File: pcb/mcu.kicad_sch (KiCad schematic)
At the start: 32 parts, among them J1 Conn_01x02_Pin, SW2 SW_Push, SW3 SW_SPDT, U1 TLV1117LV33DCYR, U2 W25Q64JVSSIQ_C179171, U3 STM32H750VBTx, Y1 25 MHz

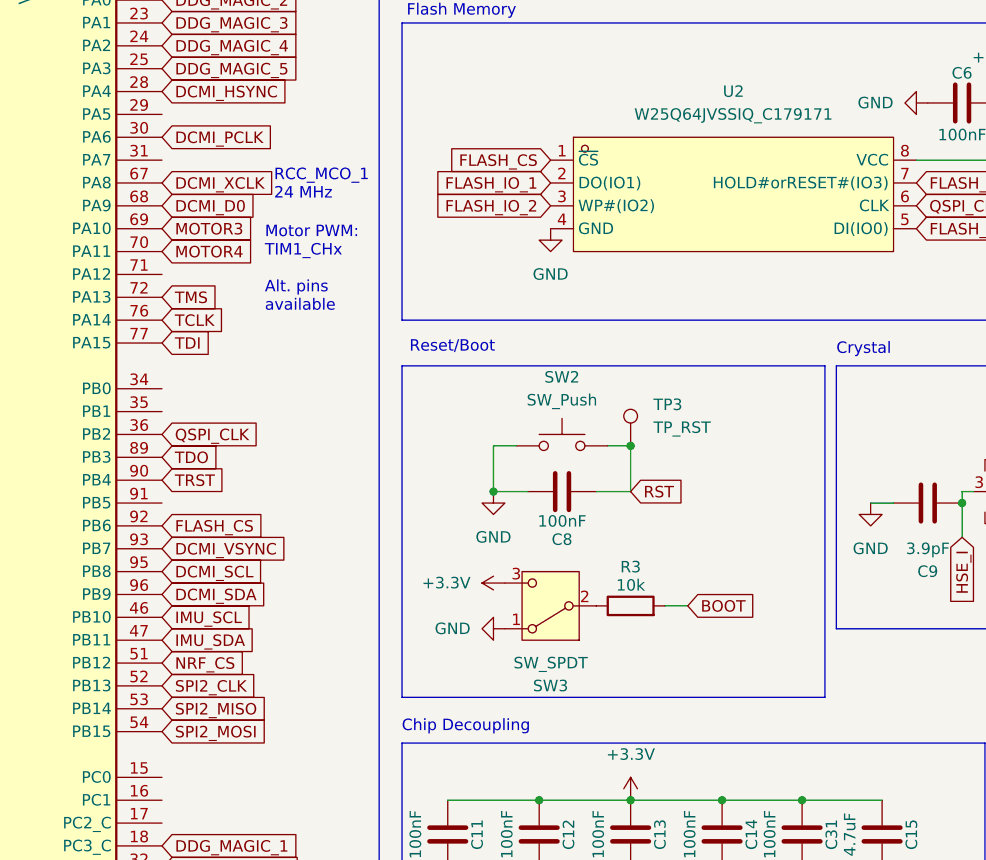
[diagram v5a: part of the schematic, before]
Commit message: [pcb] changed switches to optimize pcb layout
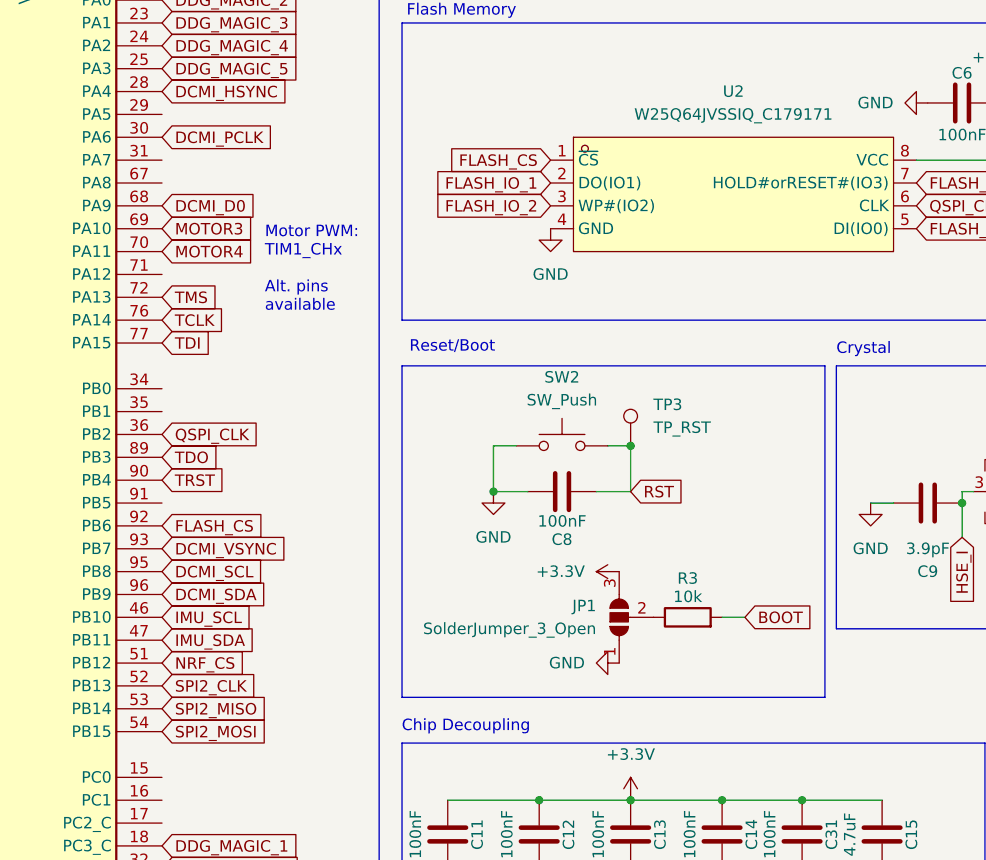
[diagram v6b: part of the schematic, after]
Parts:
- removed SW3: SW_SPDT, Button_Switch_THT:SW_Slide-03_Wuerth-WS-SLTV_10x2.5x6.4_P2.54mm, symbol Switch:SW_SPDT
- added JP1: SolderJumper_3_Open, Jumper:SolderJumper-3_P1.3mm_Open_RoundedPad1.0x1.5mm, symbol Jumper:SolderJumper_3_Open
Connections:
- net +3.3V: now also JP1.3 (B)
- net GND: now also JP1.1 (A)
- net at R3.1: now also JP1.2 (C)
- net DCMI_XCLK: no longer names the net of U3.67 (PA8)
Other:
- note removed: "RCC_MCO_1 24 MHz"
- moved on the sheet: R3
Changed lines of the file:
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@@
 		)
 	)
-	(text "RCC_MCO_1\n24 MHz"
-		(exclude_from_sim no)
-		(at 100.076 66.294 0)
-		(effects
-			(font
-				(size 1.27 1.27)
-				(color 194 0 194 1)
-			)
-			(justify left)
-		)
-	)
 	(text "SPI pins can be moved around\n\n(page 78 of datasheet)"
 		(exclude_from_sim no)
@@
 	(wire
 		(pts
-			(xy 143.51 113.03) (xy 146.05 113.03)
+			(xy 149.86 114.3) (xy 152.4 114.3)
 		)
 		(stroke
@@
 	(global_label "BOOT"
 		(shape input)
-		(at 146.05 113.03 0)
+		(at 152.4 114.3 0)
 		(fields_autoplaced yes)
 		(effects
@@
 		)
 		(property "Intersheetrefs" "${INTERSHEET_REFS}"
-			(at 153.9338 113.03 0)
+			(at 160.2838 114.3 0)
 			(effects
 				(font
@@
 		)
 	)
-	(global_label "DCMI_XCLK"
-		(shape input)
-		(at 87.63 66.04 0)
-		(fields_autoplaced yes)
-		(effects
-			(font
-				(size 1.27 1.27)
-			)
-			(justify left)
-		)
-		(property "Intersheetrefs" "${INTERSHEET_REFS}"
-			(at 100.9566 66.04 0)
-			(effects
-				(font
-					(size 1.27 1.27)
-				)
-				(justify left)
-				(hide yes)
-			)
-		)
-	)
 	(global_label "FLASH_IO_3"
 		(shape input)
@@
 	(symbol
 		(lib_id "power:GND")
-		(at 125.73 115.57 270)
+		(at 138.43 119.38 270)
 		(unit 1)
 		(exclude_from_sim no)
@@
 		(fields_autoplaced yes)
 		(property "Reference" "#PWR025"
-			(at 119.38 115.57 0)
+			(at 132.08 119.38 0)
 			(effects
 				(font
@@
 		)
 		(property "Value" "GND"
-			(at 121.92 115.5699 90)
+			(at 134.62 119.3799 90)
 			(effects
 				(font
@@
 		)
 		(property "Footprint" ""
-			(at 125.73 115.57 0)
+			(at 138.43 119.38 0)
 			(effects
 				(font
@@
 		)
 		(property "Datasheet" ""
-			(at 125.73 115.57 0)
+			(at 138.43 119.38 0)
 			(effects
 				(font
@@
 		)
 		(property "Description" "Power symbol creates a global label with name \"GND\" , ground"
-			(at 125.73 115.57 0)
+			(at 138.43 119.38 0)
 			(effects
 				(font
@@
 	)
 	(symbol
+		(lib_id "Jumper:SolderJumper_3_Open")
+		(at 138.43 114.3 90)
+		(unit 1)
+		(exclude_from_sim no)
+		(in_bom no)
+		(on_board yes)
+		(dnp no)
+		(fields_autoplaced yes)
+		(property "Reference" "JP1"
+			(at 135.89 113.0299 90)
+			(effects
+				(font
+					(size 1.27 1.27)
+				)
+				(justify left)
+			)
+		)
+		(property "Value" "SolderJumper_3_Open"
+			(at 135.89 115.5699 90)
+			(effects
+				(font
+					(size 1.27 1.27)
+				)
+				(justify left)
+			)
+		)
+		(property "Footprint" "Jumper:SolderJumper-3_P1.3mm_Open_RoundedPad1.0x1.5mm"
+			(at 138.43 114.3 0)
+			(effects
+				(font
+					(size 1.27 1.27)
+				)
+				(hide yes)
+			)
+		)
+		(property "Datasheet" "~"
+			(at 138.43 114.3 0)
+			(effects
+				(font
+					(size 1.27 1.27)
+				)
+				(hide yes)
+			)
+		)
+		(property "Description" "Solder Jumper, 3-pole, open"
+			(at 138.43 114.3 0)
+			(effects
+				(font
+					(size 1.27 1.27)
+				)
+				(hide yes)
+			)
+		)
+		(pin "1"
+		)
+		(pin "2"
+		)
+		(pin "3"
+		)
+		(instances
+			(project ""
+				(path "/c0be3de2-9de4-4447-aa6f-537ea5f31aac/0c8c942c-f992-4664-b7a3-b87cb51e1584"
+					(reference "JP1")
+					(unit 1)
+				)
+			)
+		)
+	)
+	(symbol
 		(lib_id "power:GND")
 		(at 130.81 71.12 0)
@@
 	(symbol
 		(lib_id "power:+3.3V")
-		(at 125.73 110.49 90)
+		(at 138.43 109.22 90)
 		(unit 1)
 		(exclude_from_sim no)
@@
 		(fields_autoplaced yes)
 		(property "Reference" "#PWR072"
-			(at 129.54 110.49 0)
+			(at 142.24 109.22 0)
 			(effects
 				(font
@@
 		)
 		(property "Value" "+3.3V"
-			(at 121.92 110.4899 90)
+			(at 134.62 109.2199 90)
 			(effects
 				(font
@@
 		)
 		(property "Footprint" ""
-			(at 125.73 110.49 0)
+			(at 138.43 109.22 0)
 			(effects
 				(font
@@
 		)
 		(property "Datasheet" ""
-			(at 125.73 110.49 0)
+			(at 138.43 109.22 0)
 			(effects
 				(font
@@
 		)
 		(property "Description" "Power symbol creates a global label with name \"+3.3V\""
-			(at 125.73 110.49 0)
+			(at 138.43 109.22 0)
 			(effects
 				(font
@@
 	(symbol
 		(lib_id "Device:R")
-		(at 139.7 113.03 90)
+		(at 146.05 114.3 90)
 		(unit 1)
 		(exclude_from_sim no)
@@
 		(dnp no)
 		(property "Reference" "R3"
-			(at 139.7 108.712 90)
+			(at 146.05 109.982 90)
 			(effects
 				(font
@@
 		)
 		(property "Value" "10k"
-			(at 139.7 110.744 90)
+			(at 146.05 112.014 90)
 			(effects
 				(font
@@
 		)
 		(property "Footprint" "Resistor_SMD:R_0805_2012Metric_Pad1.20x1.40mm_HandSolder"
-			(at 139.7 114.808 90)
+			(at 146.05 116.078 90)
 			(effects
 				(font
@@
 		)
 		(property "Datasheet" "~"
-			(at 139.7 113.03 0)
+			(at 146.05 114.3 0)
 			(effects
 				(font
@@
 		)
 		(property "Description" "Resistor"
-			(at 139.7 113.03 0)
+			(at 146.05 114.3 0)
 			(effects
 				(font
@@
 					(unit 1)
 				)
-			)
-		)
-	)
-	(symbol
-		(lib_id "Switch:SW_SPDT")
-		(at 130.81 113.03 180)
-		(unit 1)
-		(exclude_from_sim no)
-		(in_bom yes)
-		(on_board yes)
-		(dnp no)
-		(property "Reference" "SW3"
-			(at 130.81 121.92 0)
-			(effects
-				(font
-					(size 1.27 1.27)
-				)
-			)
-		)
-		(property "Value" "SW_SPDT"
-			(at 130.81 119.38 0)
-			(effects
-				(font
-					(size 1.27 1.27)
-				)
-			)
-		)
-		(property "Footprint" "Button_Switch_THT:SW_Slide-03_Wuerth-WS-SLTV_10x2.5x6.4_P2.54mm"
-			(at 130.81 113.03 0)
-			(effects
-				(font
-					(size 1.27 1.27)
-				)
-				(hide yes)
-			)
-		)
-		(property "Datasheet" "~"
-			(at 130.81 105.41 0)
-			(effects
-				(font
-					(size 1.27 1.27)
-				)
-				(hide yes)
-			)
-		)
-		(property "Description" "Switch, single pole double throw"
-			(at 130.81 113.03 0)
-			(effects
-				(font
-					(size 1.27 1.27)
-				)
-				(hide yes)
-			)
-		)
-		(pin "2"
-		)
-		(pin "3"
-		)
-		(pin "1"
-		)
-		(instances
-			(project "astra"
-				(path "/c0be3de2-9de4-4447-aa6f-537ea5f31aac/0c8c942c-f992-4664-b7a3-b87cb51e1584"
-					(reference "SW3")
-					(unit 1)
-				)

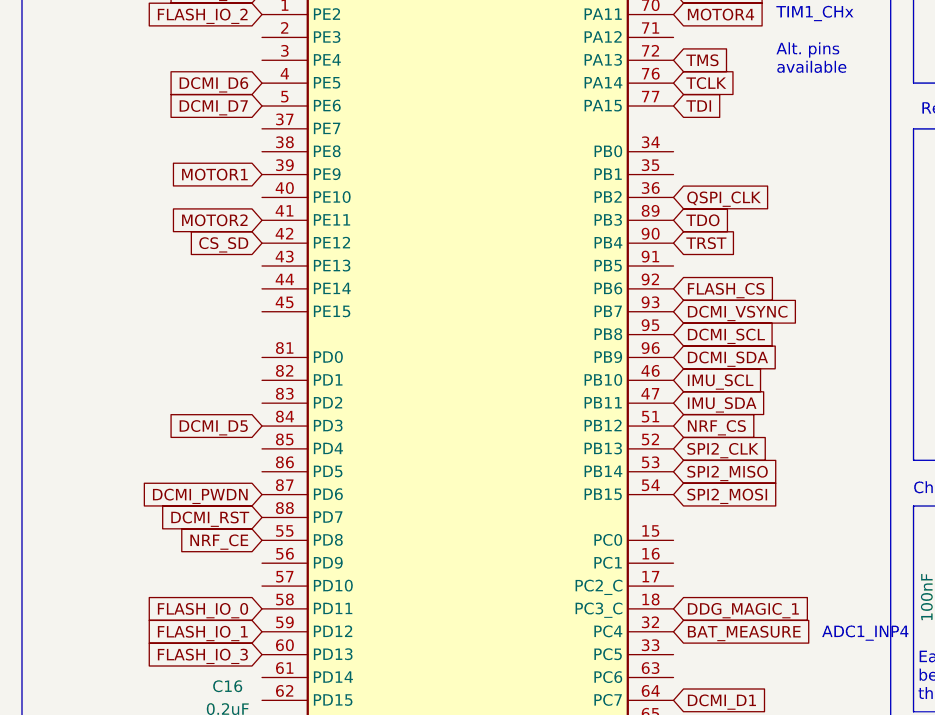
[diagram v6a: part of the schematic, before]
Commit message: [pcb] finish routing
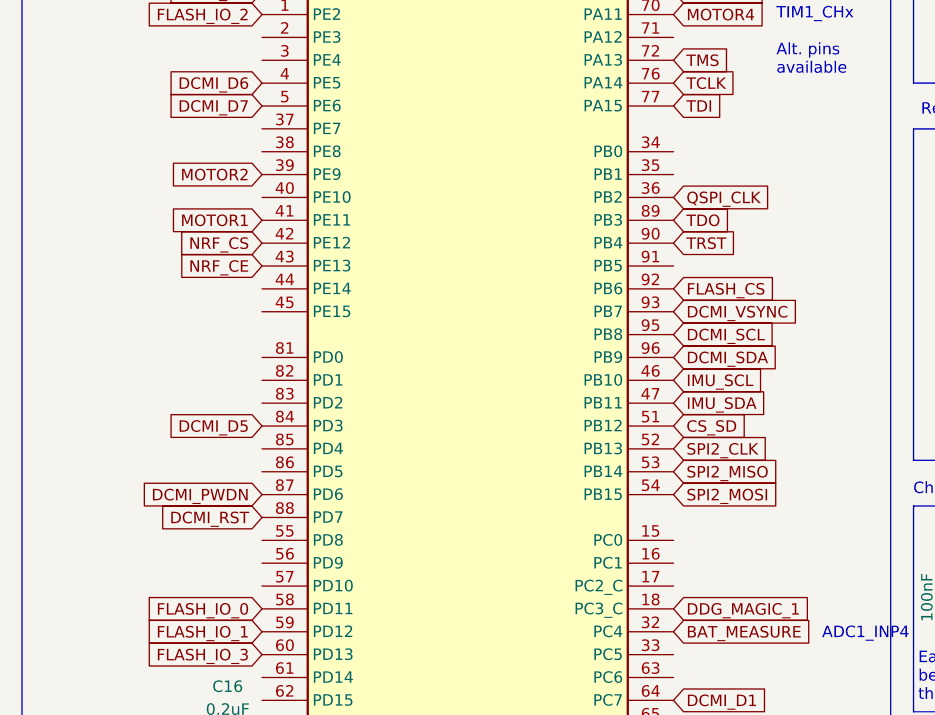
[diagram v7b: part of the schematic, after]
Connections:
- net CS_SD: now also U3.51 (PB12); no longer U3.42 (PE12)
- net MOTOR1: now also U3.41 (PE11); no longer U3.39 (PE9)
- net MOTOR2: now also U3.39 (PE9); no longer U3.41 (PE11)
- net NRF_CE: now also U3.43 (PE13); no longer U3.55 (PD8)
- net NRF_CS: now also U3.42 (PE12); no longer U3.51 (PB12)

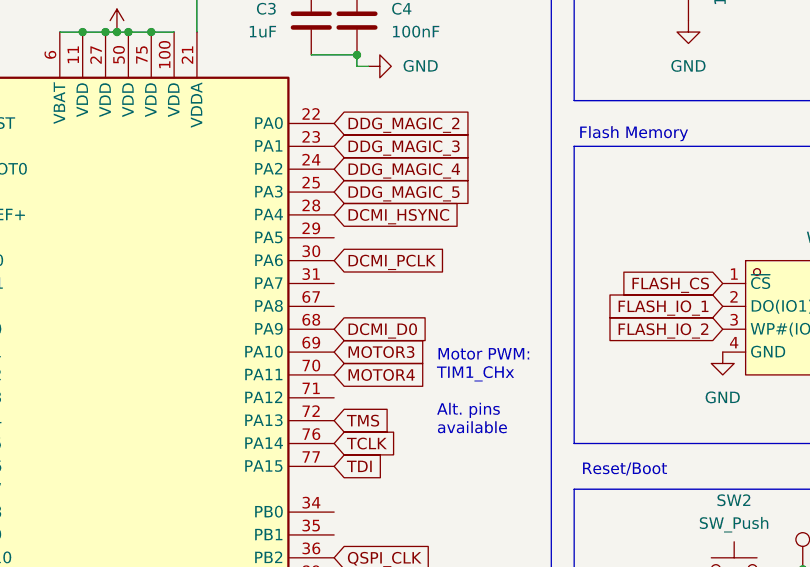
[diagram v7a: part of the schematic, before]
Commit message: [pcb] add status led
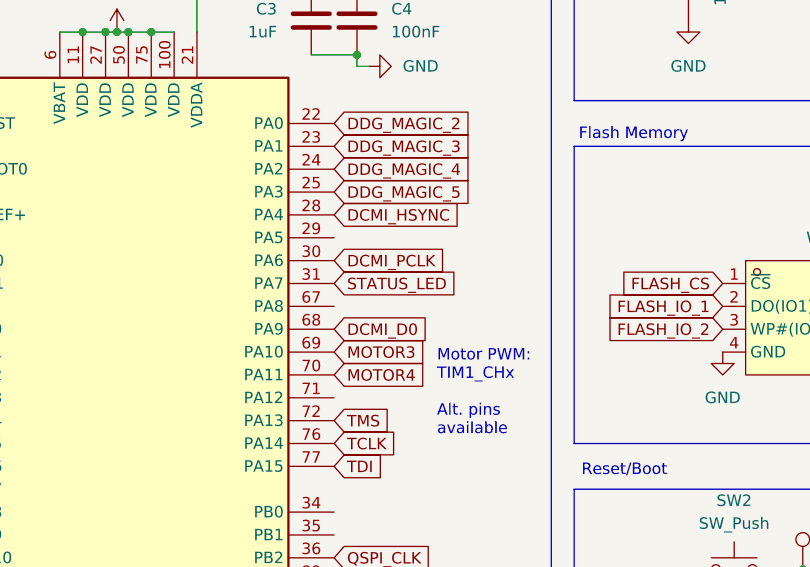
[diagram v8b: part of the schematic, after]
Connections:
- net STATUS_LED: now reaches U3.31 (PA7)
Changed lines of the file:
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@@
+		)
+	)
+	(global_label "STATUS_LED"
+		(shape input)
+		(at 87.63 63.5 0)
+		(fields_autoplaced yes)
+		(effects
+			(font
+				(size 1.27 1.27)
+			)
+			(justify left)
+		)
+		(property "Intersheetrefs" "${INTERSHEET_REFS}"
+			(at 101.8032 63.5 0)
+			(effects
+				(font
+					(size 1.27 1.27)
+				)
+				(justify left)
+				(hide yes)
+			)
 		)
 	)
